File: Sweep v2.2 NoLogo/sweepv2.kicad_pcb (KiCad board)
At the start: 2 copper layers, 216.9 x 86.9 mm, 51 parts, among them J1 AudioJack4dpb, J2 AudioJack4dpb, SW10 SW_Push, SW11 SW_Push, SW11_r1 SW_Push, SW12 SW_Push, SW12_r1 SW_Push, SW13_r1 SW_Push, SW14 SW_Push, SW15 SW_Push, SW15_r1 SW_Push, SW16 SW_Push, SW16_r1 SW_Push, SW17 SW_Push, SW17_r1 SW_Push, SW18 SW_Push, SW18_r1 SW_Push, SW2 SW_Push, SW20 SW_Push, SW20_r1 SW_Push, SW21 SW_Push, SW21_r1 SW_Push, SW2_r1 SW_Push, SW3 SW_Push, SW3_r1 SW_Push, SW4 SW_Push, SW4_r1 SW_Push, SW5 SW_Push, SW5_r1 SW_Push, SW6 SW_Push, SW6_r1 SW_Push, SW7_r1 SW_Push, SW8 SW_Push, SW8_r1 SW_Push, SW9 SW_Push, SW9_r1 SW_Push, U1 ProMicro-kbd, U2 ProMicro-kbd

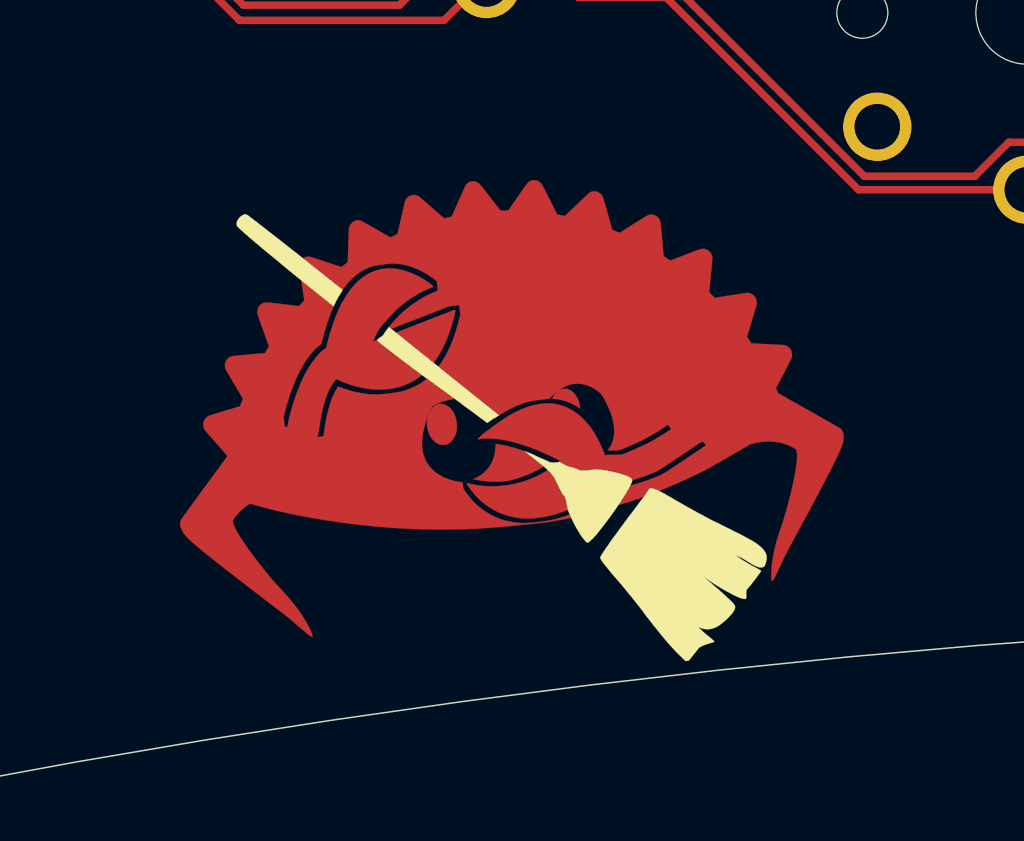
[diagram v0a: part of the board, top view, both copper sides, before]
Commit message: feat(sweep_v2_2_nologo): remove Ferris logo from PCB
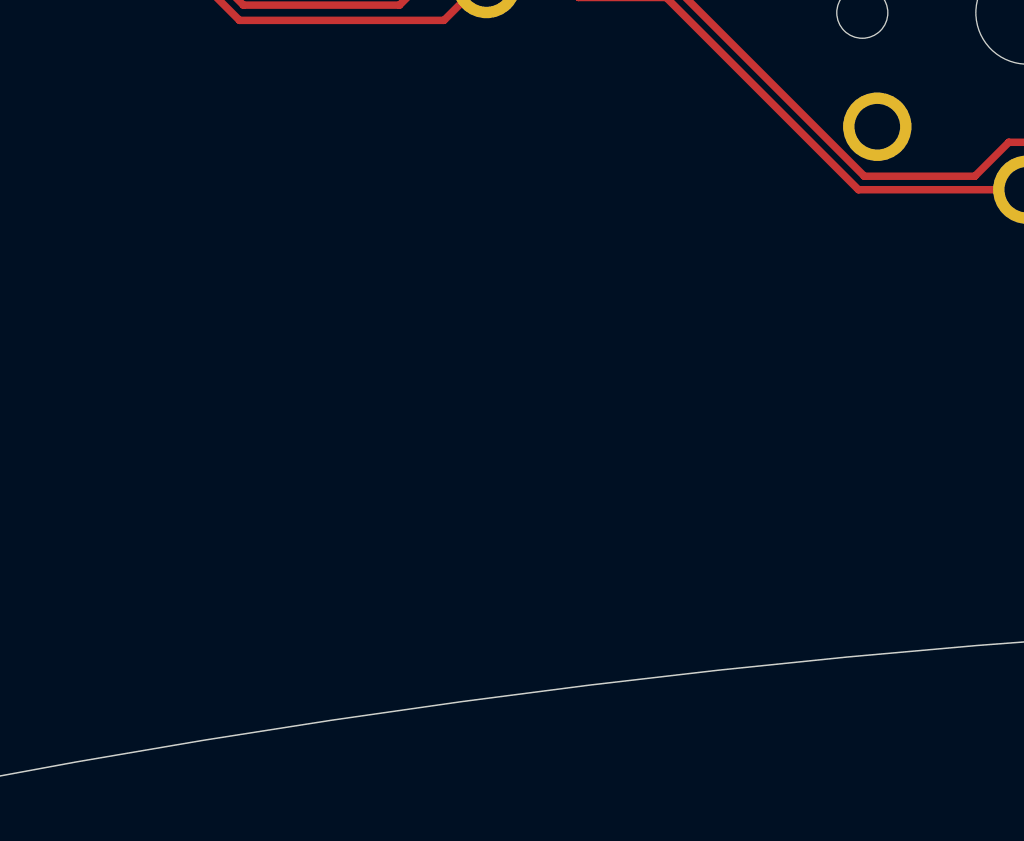
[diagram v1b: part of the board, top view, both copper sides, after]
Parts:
- removed G***: LOGO, Kailh:ferris_broom
